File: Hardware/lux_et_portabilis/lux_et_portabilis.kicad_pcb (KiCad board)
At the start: 2 copper layers, 63 x 43 mm, 35 parts, among them J1 Conn_01x03_Socket, J2 Conn_01x03_Socket, J3 Conn_01x04_Socket, Q1 2N7002K, U1 ESP32-C3-Supermini, U2 TP4056

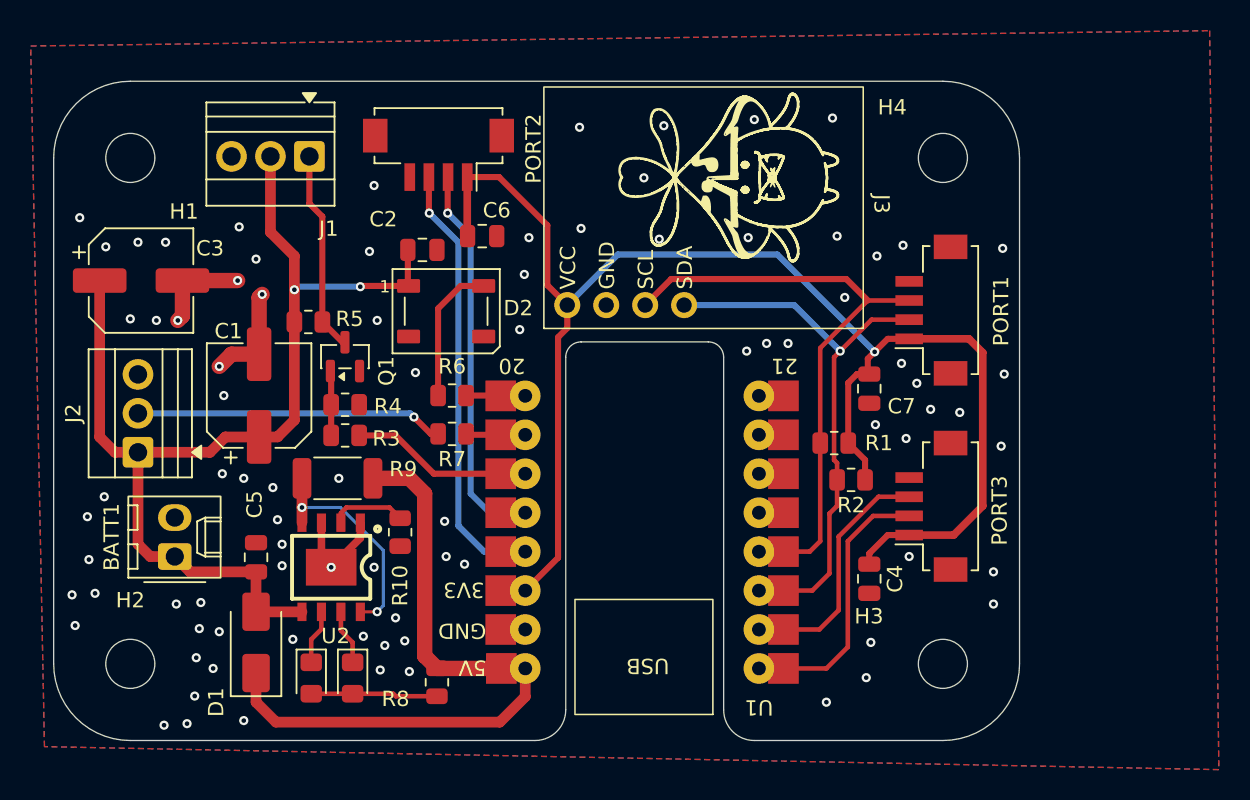
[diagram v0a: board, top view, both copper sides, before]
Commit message: Update on fabrication files
Added serial header
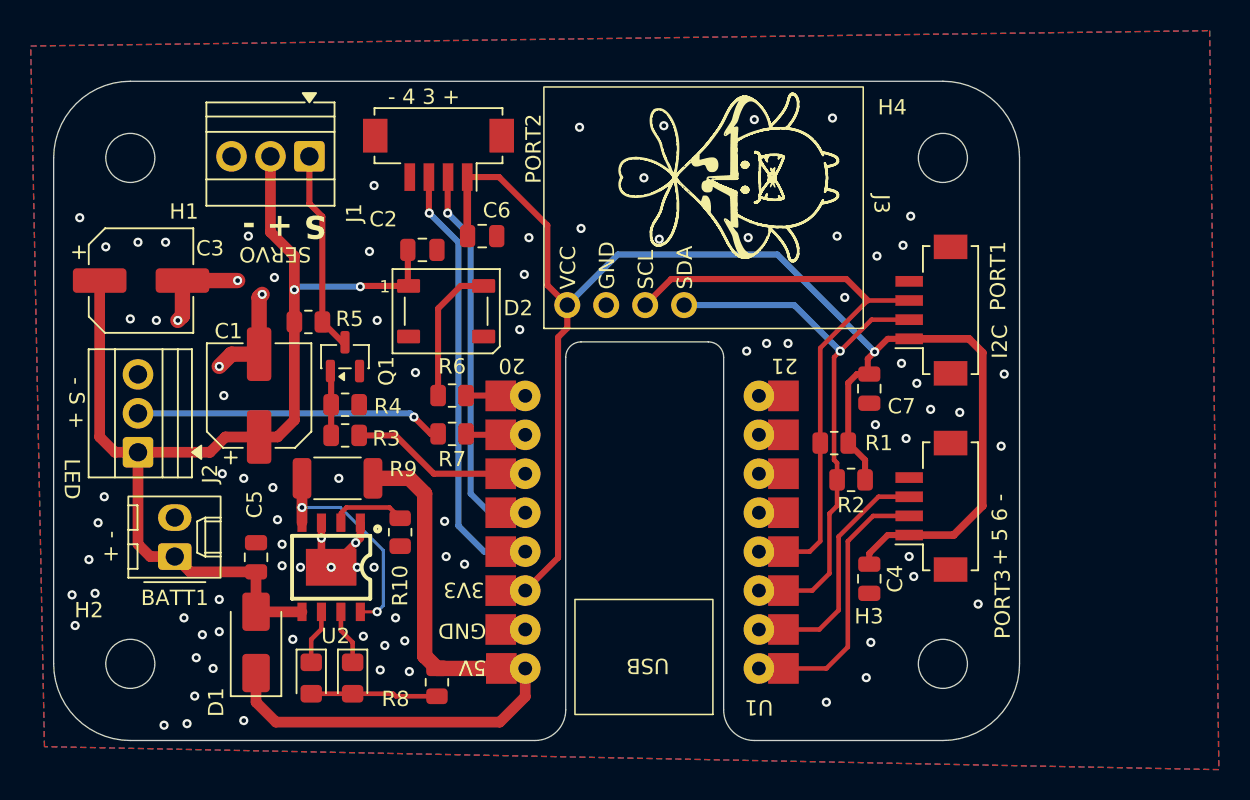
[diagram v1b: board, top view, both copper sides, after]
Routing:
- net GND: vias 85 -> 89
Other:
- board text added: "+ -"
- board text added: "+ 5 6 -"
- board text added: "- 4 3 +"
- board text added: "- S +"
- board text added: "I2C"
- board text added: "LED"
- board text added: "S + -"
- board text added: "SERVO"
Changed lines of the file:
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@@
 		(tags "mountinghole M3")
 		(property "Reference" "H2"
-			(at 0 -4.15 0)
+			(at -2.7 -3.5 0)
 			(layer "F.SilkS")
 			(effects
@@
 		(tags "connector Hirose DF13C vertical")
 		(property "Reference" "PORT3"
-			(at -0.275 4.45 90)
+			(at -6.375 4.65 90)
 			(layer "F.SilkS")
 			(effects
@@
 		(tags "connector Hirose DF13C vertical")
 		(property "Reference" "PORT1"
-			(at -0.075 4.55 90)
+			(at 2.225 4.35 270)
 			(layer "F.SilkS")
 			(effects
@@
 		(tags "THT Terminal Block Xinya XY308-2.54-3P pitch 2.54mm size 8.12x6.5mm drill 1.2mm pad 2mm")
 		(property "Reference" "J2"
-			(at 2.54 -4.22 90)
+			(at -1.4 4.7 270)
 			(layer "F.SilkS")
 			(effects
@@
 		(tags "THT Terminal Block Xinya XY308-2.54-3P pitch 2.54mm size 8.12x6.5mm drill 1.2mm pad 2mm")
 		(property "Reference" "J1"
-			(at -1.255 -4.7175 0)
+			(at -2.92 -3.7 90)
 			(layer "F.SilkS")
 			(effects
@@
 		(tags "connector Molex KK-254 vertical")
 		(property "Reference" "BATT1"
-			(at 1.27 -4.12 90)
+			(at -2.7 0 180)
 			(layer "F.SilkS")
 			(effects
@@
 		(layer "Edge.Cuts")
 	)
+	(gr_text "+ 5 6 -"
+		(at 171.8 106.7 90)
+		(layer "F.SilkS")
+		(effects
+			(font
+				(size 1 1)
+				(thickness 0.1)
+			)
+			(justify left bottom)
+		)
+	)
+	(gr_text "LED"
+		(at 110.1 99.7 270)
+		(layer "F.SilkS")
+		(effects
+			(font
+				(size 1 1)
+				(thickness 0.1)
+			)
+			(justify left bottom)
+		)
+	)
+	(gr_text "S + -"
+		(at 127.3 83.7 180)
+		(layer "F.SilkS")
+		(effects
+			(font
+				(size 1.5 1.5)
+				(thickness 0.3)
+				(bold yes)
+			)
+			(justify left bottom)
+		)
+	)
+	(gr_text "- S +"
+		(at 110.4 94.4 270)
+		(layer "F.SilkS")
+		(effects
+			(font
+				(size 1 1)
+				(thickness 0.1)
+			)
+			(justify left bottom)
+		)
+	)
+	(gr_text "I2C"
+		(at 171.8 93.2 90)
+		(layer "F.SilkS")
+		(effects
+			(font
+				(size 1 1)
+				(thickness 0.1)
+			)
+			(justify left bottom)
+		)
+	)
+	(gr_text "+ -"
+		(at 113.8 106.5 90)
+		(layer "F.SilkS")
+		(effects
+			(font
+				(size 1 1)
+				(thickness 0.1)
+			)
+			(justify left bottom)
+		)
+	)
+	(gr_text "SERVO"
+		(at 126.3 85.8 180)
+		(layer "F.SilkS")
+		(effects
+			(font
+				(size 1 1)
+				(thickness 0.1)
+			)
+			(justify left bottom)
+		)
+	)
+	(gr_text "- 4 3 +"
+		(at 131.3 76.7 0)
+		(layer "F.SilkS")
+		(effects
+			(font
+				(size 1 1)
+				(thickness 0.1)
+			)
+			(justify left bottom)
+		)
+	)
 	(segment
 		(start 117.9 88.1)
@@
 	(segment
 		(start 129.505 104.895)
-		(end 127.6 106.8)
+		(end 129.2 105.2)
 		(width 0.5)
 		(layer "F.Cu")
@@
 	(segment
 		(start 126.965 103.8915)
-		(end 126.965 106.165)
+		(end 126.965 104.9)
 		(width 0.5)
 		(layer "F.Cu")
@@
 	)
 	(segment
+		(start 129.2 105.2)
+		(end 127.6 106.8)
+		(width 0.5)
+		(layer "F.Cu")
+		(net 1)
+	)
+	(segment
 		(start 122.9 92.9)
 		(end 122.9 89.2)
@@
 	)
 	(segment
+		(start 126.965 104.9)
+		(end 126.965 106.165)
+		(width 0.5)
+		(layer "F.Cu")
+		(net 1)
+	)
+	(segment
 		(start 117.9 88.1)
 		(end 117.9 90.4)
@@
 	)
 	(via
+		(at 129.2 105.2)
+		(size 0.6)
+		(drill 0.3)
+		(layers "F.Cu" "B.Cu")
+		(net 1)
+	)
+	(via
 		(at 130.1 86.2)
 		(size 0.6)
@@
 	)
 	(via
-		(at 111.7 103.5)
+		(at 112.4 103.9)
 		(size 0.6)
 		(drill 0.3)
@@
 	)
 	(via
-		(at 170.8 109.2)
+		(at 169.8 109.2)
 		(size 0.6)
 		(drill 0.3)
@@
 	)
 	(via
+		(at 126.965 104.9)
+		(size 0.6)
+		(drill 0.3)
+		(layers "F.Cu" "B.Cu")
+		(net 1)
+	)
+	(via
 		(at 140.5 85.3)
 		(size 0.6)
@@
 	)
 	(via
-		(at 117.5 109.2)
+		(at 118 110.1)
 		(size 0.6)
 		(drill 0.3)
@@
 	)
 	(via
-		(at 171.4 86)
+		(at 165.4 83.9)
 		(size 0.6)
 		(drill 0.3)
@@
 	)
 	(via
+		(at 125.6 106.8)
+		(size 0.6)
+		(drill 0.3)
+		(layers "F.Cu" "B.Cu")
+		(free yes)
+		(net 1)
+	)
+	(via
 		(at 165.8 94.8)
 		(size 0.6)
@@
 	)
 	(via
-		(at 119.1 109.1)
+		(at 120.3 108.9)
 		(size 0.6)
 		(drill 0.3)
@@
 	)
 	(via
-		(at 119 110.8)
+		(at 119.2 111.2)
 		(size 0.6)
 		(drill 0.3)
@@
 	)
 	(via
-		(at 122.7 86.7)
+		(at 123.9 87.9)
 		(size 0.6)
 		(drill 0.3)
@@
 	)
 	(via
-		(at 170.8 107.1)
+		(at 165.6 107.4)
 		(size 0.6)
 		(drill 0.3)
@@
 	)
 	(via
-		(at 121.6 84.6)
+		(at 122.2 85.2)
 		(size 0.6)
 		(drill 0.3)
@@
 		(size 0.6)
 		(drill 0.3)
+		(layers "F.Cu" "B.Cu")
+		(free yes)
+		(net 1)
+	)
+	(via
+		(at 129.3 106.8)
+		(size 0.6)
+		(drill 0.3)

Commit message: Fabrication files update
Removed copper fill near WiFi antenna
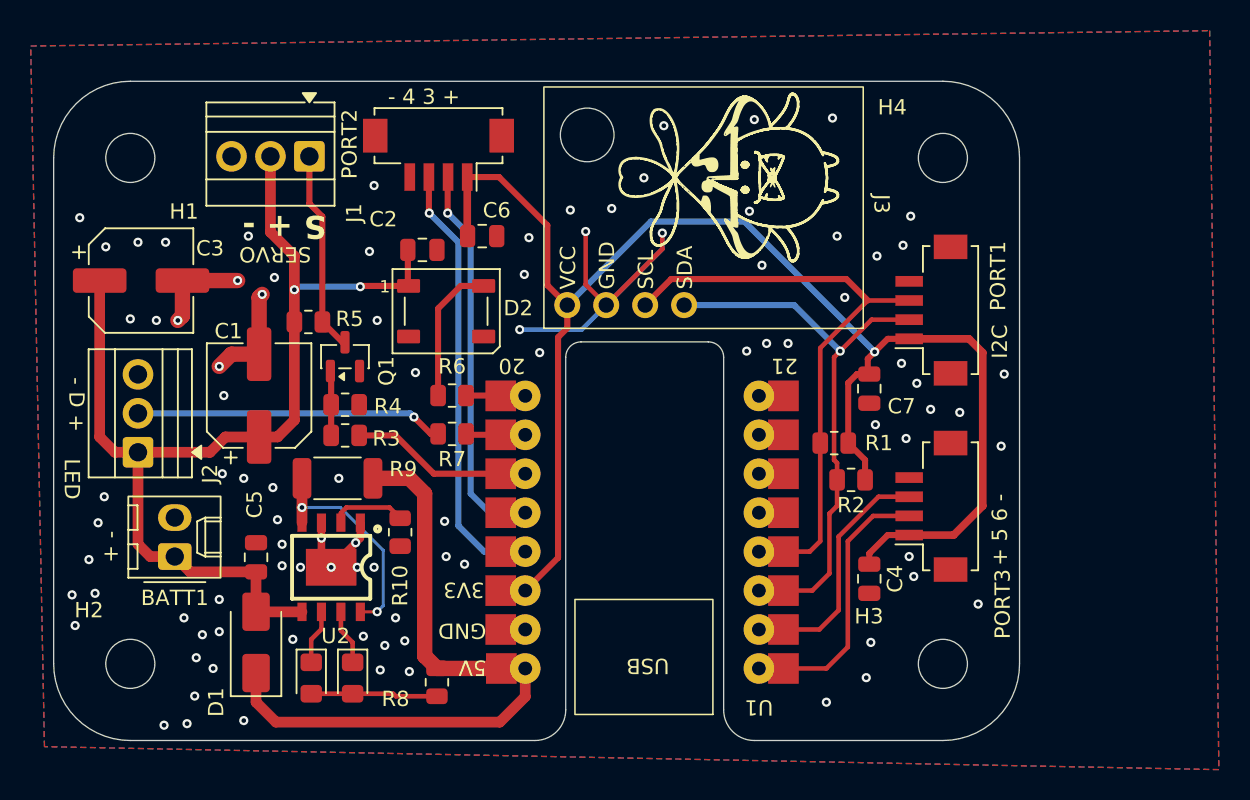
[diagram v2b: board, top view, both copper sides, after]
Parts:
- added REF**: MountingHole_3.5mm, MountingHole:MountingHole_3.5mm, F.Cu at (144.3, 78.6)
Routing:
- net GND: track 20.1 -> 44.2 mm, vias 89 -> 92
- net +3.3V: track 97.1 -> 98.9 mm
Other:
- board text added: "- D +"
- board text removed: "- S +"
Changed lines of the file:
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@@
 		)
 	)
+	(footprint "MountingHole:MountingHole_3.5mm"
+		(layer "F.Cu")
+		(at 144.3 78.6)
+		(descr "Mounting Hole 3.5mm, no annular, generated by kicad-footprint-generator mountinghole.py")
+		(tags "mountinghole")
+		(property "Reference" "REF**"
+			(at 0 -4.45 0)
+			(layer "F.SilkS")
+			(hide yes)
+			(effects
+				(font
+					(size 1 1)
+					(thickness 0.15)
+				)
+			)
+		)
+		(property "Value" "MountingHole_3.5mm"
+			(at 0 4.45 0)
+			(layer "F.Fab")
+			(effects
+				(font
+					(size 1 1)
+					(thickness 0.15)
+				)
+			)
+		)
+		(property "Datasheet" ""
+			(at 0 0 0)
+			(layer "F.Fab")
+			(hide yes)
+			(effects
+				(font
+					(size 1.27 1.27)
+					(thickness 0.15)
+				)
+			)
+		)
+		(property "Description" ""
+			(at 0 0 0)
+			(layer "F.Fab")
+			(hide yes)
+			(effects
+				(font
+					(size 1.27 1.27)
+					(thickness 0.15)
+				)
+			)
+		)
+		(attr board_only exclude_from_pos_files exclude_from_bom)
+		(fp_circle
+			(center 0 0)
+			(end 3.5 0)
+			(stroke
+				(width 0.15)
+				(type solid)
+			)
+			(fill no)
+			(layer "Cmts.User")
+		)
+		(fp_circle
+			(center 0 0)
+			(end 3.75 0)
+			(stroke
+				(width 0.05)
+				(type solid)
+			)
+			(fill no)
+			(layer "F.CrtYd")
+		)
+		(fp_text user "${REFERENCE}"
+			(at 0 0 0)
+			(layer "F.Fab")
+			(effects
+				(font
+					(size 1 1)
+					(thickness 0.15)
+				)
+			)
+		)
+		(pad "" np_thru_hole circle
+			(at 0 0)
+			(size 3.5 3.5)
+			(drill 3.5)
+			(layers "*.Cu" "*.Mask")
+		)
+		(embedded_fonts no)
+	)
 	(footprint "MountingHole:MountingHole_3.2mm_M3"
 		(layer "F.Cu")
@@
 		(tags "connector Hirose DF13C vertical")
 		(property "Reference" "PORT2"
-			(at -6.2 0.4 90)
+			(at 5.8 0.7 90)
 			(layer "F.SilkS")
 			(effects
@@
 		)
 		(embedded_fonts no)
+		(model "C:/Users/macha/Downloads/ESP32-C3 supermini v5.step"
+			(offset
+				(xyz -12 -16.25 -2)
+			)
+			(scale
+				(xyz 1 1 1)
+			)
+			(rotate
+				(xyz -90 -0 -180)
+			)
+		)
 	)
 	(footprint "TerminalBlock:TerminalBlock_Xinya_XY308-2.54-3P_1x03_P2.54mm_Horizontal"
@@
 		)
 	)
-	(gr_text "- S +"
+	(gr_text "- D +"
 		(at 110.4 94.4 270)
 		(layer "F.SilkS")
@@
 	)
 	(segment
+		(start 149.2 86.04)
+		(end 149.2 85)
+		(width 0.3)
+		(layer "F.Cu")
+		(net 1)
+	)
+	(segment
 		(start 121.1 92.9)
 		(end 120.3 93.7)
@@
 	)
 	(segment
+		(start 145.54 89.7)
+		(end 144.2 88.36)
+		(width 0.3)
+		(layer "F.Cu")
+		(net 1)
+	)
+	(segment
+		(start 145.54 89.7)
+		(end 149.2 86.04)
+		(width 0.3)
+		(layer "F.Cu")
+		(net 1)
+	)
+	(segment
 		(start 122.9 92.9)
 		(end 122.9 89.2)
@@
 		(net 1)
 	)
+	(segment
+		(start 144.2 88.36)
+		(end 144.2 84.9)
+		(width 0.3)
+		(layer "F.Cu")
+		(net 1)
+	)
 	(via
 		(at 116.2 90.7)
@@
 	)
 	(via
-		(at 143.8 78.1)
-		(size 0.6)
-		(drill 0.3)
-		(layers "F.Cu" "B.Cu")
-		(free yes)
-		(net 1)
-	)
-	(via
 		(at 126.965 104.9)
 		(size 0.6)
@@
 	)
 	(via
+		(at 141.2 92.8)
+		(size 0.6)
+		(drill 0.3)
+		(layers "F.Cu" "B.Cu")
+		(free yes)
+		(net 1)
+	)
+	(via
+		(at 144.2 84.9)
+		(size 0.6)
+		(drill 0.3)
+		(layers "F.Cu" "B.Cu")
+		(net 1)
+	)
+	(via
 		(at 130.4 81.9)
 		(size 0.6)
@@
 	)
 	(via
-		(at 154.8 85.3)
+		(at 154.882272 83.577619)
 		(size 0.6)
 		(drill 0.3)
@@
 	)
 	(via
-		(at 149 85.4)
+		(at 145.9 83.4)
 		(size 0.6)
 		(drill 0.3)
@@
 	)
 	(via
+		(at 155.7 87.1)
+		(size 0.6)
+		(drill 0.3)
+		(layers "F.Cu" "B.Cu")
+		(free yes)
+		(net 1)
+	)
+	(via
 		(at 120.5 100.7)
 		(size 0.6)
@@
 	)
 	(via
+		(at 149.2 85)
+		(size 0.6)
+		(drill 0.3)
+		(layers "F.Cu" "B.Cu")
+		(net 1)
+	)
+	(via
 		(at 112.2 108.5)
 		(size 0.6)
@@
 	)
 	(via
-		(at 143.9 84.7)
+		(at 143.2 83.5)
 		(size 0.6)
 		(drill 0.3)
@@
 	)
 	(segment
+		(start 149.2 86.04)
+		(end 149.2 85)
+		(width 0.3)
+		(layer "B.Cu")
+		(net 1)
+	)
+	(segment
+		(start 145.54 89.7)
+		(end 149.2 86.04)
+		(width 0.3)
+		(layer "B.Cu")
+		(net 1)
+	)
+	(segment
+		(start 145.54 89.7)
+		(end 143.94 91.3)
+		(width 0.3)
+		(layer "B.Cu")
+		(net 1)
+	)
+	(segment
+		(start 143.94 91.3)
+		(end 139.9 91.3)
+		(width 0.3)
+		(layer "B.Cu")
+		(net 1)
+	)
+	(segment
 		(start 124 116.9)
 		(end 138.6 116.9)
@@
 	)
 	(segment
-		(start 163.05 92.75)
-		(end 156.7 86.4)
+		(start 148.45 84.25)
+		(end 143 89.7)
 		(width 0.4)
 		(layer "B.Cu")
@@
 	)
 	(segment
-		(start 146.3 86.4)
-		(end 143 89.7)
+		(start 163.05 92.75)
+		(end 154.55 84.25)
 		(width 0.4)
 		(layer "B.Cu")
@@
 	)
 	(segment
-		(start 156.7 86.4)
-		(end 146.3 86.4)
+		(start 154.55 84.25)
+		(end 148.45 84.25)
 		(width 0.4)
 		(layer "B.Cu")
@@
 	)
 	(zone
+		(net 0)
+		(net_name "")
+		(layers "F.Cu" "B.Cu")
+		(hatch edge 0.5)
+		(connect_pads
+			(clearance 0)
+		)
+		(min_thickness 0.25)
+		(filled_areas_thickness no)
+		(keepout
+			(tracks allowed)
+			(vias allowed)
+			(pads allowed)
+			(copperpour not_allowed)
+			(footprints allowed)
+		)
+		(placement
+			(enabled no)
+			(sheetname "")
+		)
+		(fill
+			(thermal_gap 0.5)
+			(thermal_bridge_width 0.5)
+		)
+		(polygon
+			(pts
+				(xy 142.9 93) (xy 141.2 91.1) (xy 141.2 85.5) (xy 154.7 85.5) (xy 154.7 91.2) (xy 153.2 93)
+			)
+		)
+	)
+	(zone
